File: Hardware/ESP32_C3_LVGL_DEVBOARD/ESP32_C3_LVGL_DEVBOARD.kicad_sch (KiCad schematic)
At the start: 62 parts, among them J1 CONN_USBC, J2 CONN_UART, J3 Conn_Coaxial, SW1 SW_Push_SPST_4Pads, SW2 SW_Push_SPST_4Pads, U2 USBLC6-2SC6, U3 AMS1117-3.3, U4 ESP32-C3, U5 Winbond-W25Q64JVSSIQ, U6 USBLC6-2SC6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

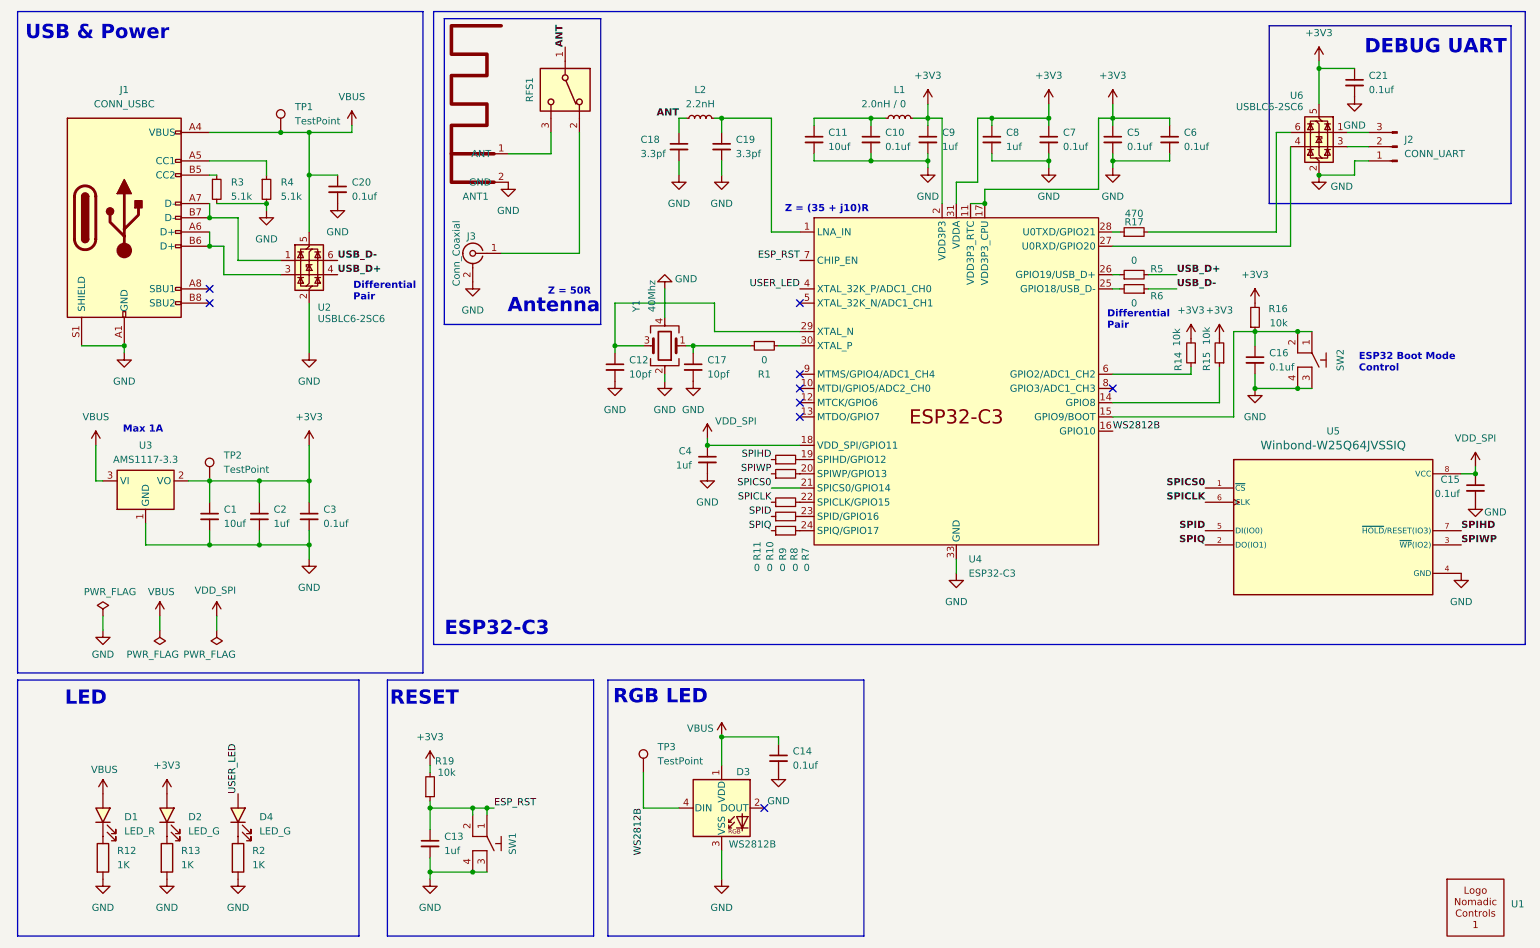
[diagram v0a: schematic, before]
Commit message: updated pcb with placement & basic routing
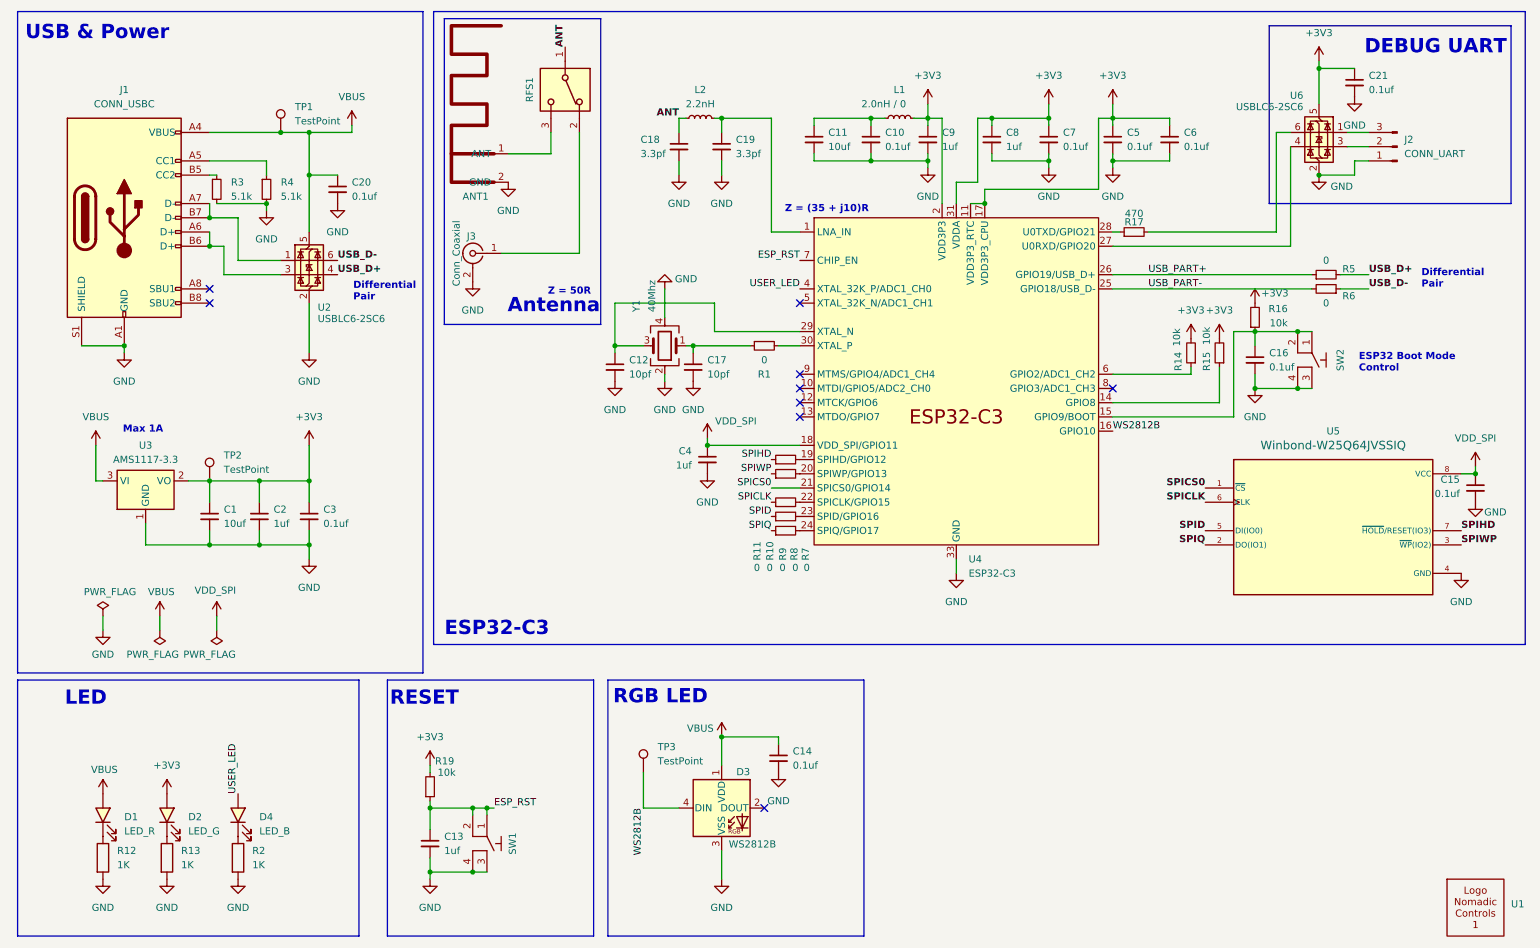
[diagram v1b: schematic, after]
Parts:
- C10, C14, C15, C16, C20, C21, C3, C5, C6, C7: footprint Capacitor_SMD:C_0805_2012Metric -> Capacitor_SMD:C_0603_1608Metric
- C12, C17: footprint Capacitor_SMD:C_0402_1005Metric -> Capacitor_SMD:C_0603_1608Metric
- D4: value LED_G -> LED_B
- L1: footprint Inductor_SMD:L_0805_2012Metric -> Inductor_SMD:L_0603_1608Metric
- R1, R10, R11, R12, R13, R14, R15, R16, R19, R2, R3, R4, R5, R6, R7, R8, R9: footprint Resistor_SMD:R_0805_2012Metric -> Resistor_SMD:R_0603_1608Metric
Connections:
- net USB_PART-: now reaches R6.2, U4.25 (GPIO18/USB_D-)
- net USB_PART+: now reaches R5.1, U4.26 (GPIO19/USB_D+)
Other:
- moved on the sheet: R5, R6
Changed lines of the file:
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@@
 	(wire
 		(pts
-			(xy 209.55 63.5) (xy 210.82 63.5)
+			(xy 209.55 63.5) (xy 245.11 63.5)
 		)
 		(stroke
@@
 	(wire
 		(pts
-			(xy 209.55 60.96) (xy 210.82 60.96)
+			(xy 209.55 60.96) (xy 245.11 60.96)
 		)
 		(stroke
@@
 	(wire
 		(pts
-			(xy 215.9 63.5) (xy 220.98 63.5)
+			(xy 250.19 63.5) (xy 255.27 63.5)
 		)
 		(stroke
@@
 	(wire
 		(pts
-			(xy 215.9 60.96) (xy 220.98 60.96)
+			(xy 250.19 60.96) (xy 255.27 60.96)
 		)
 		(stroke
@@
 	(text "Differential\nPair"
 		(exclude_from_sim no)
-		(at 208.534 69.088 0)
+		(at 264.668 61.722 0)
 		(effects
 			(font
@@
 		)
 	)
+	(label "USB_PART-"
+		(at 215.9 63.5 0)
+		(fields_autoplaced yes)
+		(effects
+			(font
+				(size 1.27 1.27)
+			)
+			(justify left bottom)
+		)
+	)
 	(label "USB_D-"
 		(at 71.12 58.42 0)
@@
 	)
 	(label "USB_D-"
-		(at 220.98 63.5 0)
+		(at 255.27 63.5 0)
 		(fields_autoplaced yes)
 		(effects
@@
 		)
 	)
+	(label "USB_PART+"
+		(at 215.9 60.96 0)
+		(fields_autoplaced yes)
+		(effects
+			(font
+				(size 1.27 1.27)
+			)
+			(justify left bottom)
+		)
+	)
 	(label "USER_LED"
 		(at 53.34 153.67 90)
@@
 	)
 	(label "USB_D+"
-		(at 220.98 60.96 0)
+		(at 255.27 60.96 0)
 		(fields_autoplaced yes)
 		(effects
@@
 			)
 		)
-		(property "Footprint" "Resistor_SMD:R_0805_2012Metric"
+		(property "Footprint" "Resistor_SMD:R_0603_1608Metric"
 			(at 49.53 45.72 0)
 			(effects
@@
 			)
 		)
-		(property "Footprint" "Capacitor_SMD:C_0402_1005Metric"
+		(property "Footprint" "Capacitor_SMD:C_0603_1608Metric"
 			(at 120.65 77.47 0)
 			(effects
@@
 			)
 		)
-		(property "Footprint" "Capacitor_SMD:C_0805_2012Metric"
+		(property "Footprint" "Capacitor_SMD:C_0603_1608Metric"
 			(at 166.37 36.83 0)
 			(effects
@@
 			)
 		)
-		(property "Footprint" "Capacitor_SMD:C_0805_2012Metric"
+		(property "Footprint" "Capacitor_SMD:C_0603_1608Metric"
 			(at 198.12 36.83 0)
 			(effects
@@
 			)
 		)
-		(property "Footprint" "Capacitor_SMD:C_0805_2012Metric"
+		(property "Footprint" "Capacitor_SMD:C_0603_1608Metric"
 			(at 66.04 104.14 0)
 			(effects
@@
 	(symbol
 		(lib_id "Device:R_Small")
-		(at 213.36 63.5 270)
+		(at 247.65 63.5 270)
 		(mirror x)
 		(unit 1)
@@
 		(dnp no)
 		(property "Reference" "R6"
-			(at 217.424 64.77 90)
+			(at 251.714 64.77 90)
 			(effects
 				(font
@@
 		)
 		(property "Value" "0"
-			(at 213.36 66.04 90)
+			(at 247.65 66.04 90)
 			(effects
 				(font
@@
 			)
 		)
-		(property "Footprint" "Resistor_SMD:R_0805_2012Metric"
-			(at 213.36 63.5 0)
+		(property "Footprint" "Resistor_SMD:R_0603_1608Metric"
+			(at 247.65 63.5 0)
 			(effects
 				(font
@@
 		)
 		(property "Datasheet" "~"
-			(at 213.36 63.5 0)
+			(at 247.65 63.5 0)
 			(effects
 				(font
@@
 		)
 		(property "Description" "Resistor, small symbol"
-			(at 213.36 63.5 0)
+			(at 247.65 63.5 0)
 			(effects
 				(font
@@
 			)
 		)
-		(property "Footprint" "Resistor_SMD:R_0805_2012Metric"
+		(property "Footprint" "Resistor_SMD:R_0603_1608Metric"
 			(at 151.13 96.52 0)
 			(effects
@@
 			)
 		)
-		(property "Footprint" "Resistor_SMD:R_0805_2012Metric"
+		(property "Footprint" "Resistor_SMD:R_0603_1608Metric"
 			(at 151.13 101.6 0)
 			(effects
@@
 			)
 		)
-		(property "Footprint" "Resistor_SMD:R_0805_2012Metric"
+		(property "Footprint" "Resistor_SMD:R_0603_1608Metric"
 			(at 151.13 93.98 0)
 			(effects
@@
 			)
 		)
-		(property "Footprint" "Resistor_SMD:R_0805_2012Metric"
+		(property "Footprint" "Resistor_SMD:R_0603_1608Metric"
 			(at 228.6 74.93 0)
 			(effects
@@
 			)
 		)
-		(property "Footprint" "Capacitor_SMD:C_0805_2012Metric"
+		(property "Footprint" "Capacitor_SMD:C_0603_1608Metric"
 			(at 209.55 36.83 0)
 			(effects
@@
 			)
 		)
-		(property "Footprint" "Resistor_SMD:R_0805_2012Metric"
+		(property "Footprint" "Resistor_SMD:R_0603_1608Metric"
 			(at 234.95 68.58 0)
 			(effects
@@
 			)
 		)
-		(property "Footprint" "Resistor_SMD:R_0805_2012Metric"
+		(property "Footprint" "Resistor_SMD:R_0603_1608Metric"
 			(at 147.32 73.66 0)
 			(effects
@@
 			)
 		)
-		(property "Footprint" "Capacitor_SMD:C_0805_2012Metric"
+		(property "Footprint" "Capacitor_SMD:C_0603_1608Metric"
 			(at 252.73 26.67 0)
 			(effects
@@
 			)
 		)
-		(property "Footprint" "Resistor_SMD:R_0805_2012Metric"
+		(property "Footprint" "Resistor_SMD:R_0603_1608Metric"
 			(at 27.432 165.1 90)
 			(effects
@@
 	(symbol
 		(lib_id "Device:R_Small")
-		(at 213.36 60.96 90)
+		(at 247.65 60.96 90)
 		(unit 1)
 		(exclude_from_sim no)
@@
 		(dnp no)
 		(property "Reference" "R5"
-			(at 217.424 59.944 90)
+			(at 251.714 59.944 90)
 			(effects
 				(font
@@
 		)
 		(property "Value" "0"
-			(at 213.36 58.42 90)
+			(at 247.65 58.42 90)
 			(effects
 				(font
@@
 			)
 		)
-		(property "Footprint" "Resistor_SMD:R_0805_2012Metric"
-			(at 213.36 60.96 0)
+		(property "Footprint" "Resistor_SMD:R_0603_1608Metric"
+			(at 247.65 60.96 0)
 			(effects
 				(font
@@
 		)
 		(property "Datasheet" "~"
-			(at 213.36 60.96 0)
+			(at 247.65 60.96 0)
 			(effects
 				(font
@@
 		)
 		(property "Description" "Resistor, small symbol"
-			(at 213.36 60.96 0)
+			(at 247.65 60.96 0)
 			(effects
 				(font
@@
 			)
 		)
-		(property "Footprint" "Resistor_SMD:R_0805_2012Metric"
+		(property "Footprint" "Resistor_SMD:R_0603_1608Metric"
 			(at 151.13 106.68 0)
 			(effects
@@
 			)
 		)
-		(property "Footprint" "Resistor_SMD:R_0805_2012Metric"
+		(property "Footprint" "Resistor_SMD:R_0603_1608Metric"
 			(at 223.52 74.93 0)
 			(effects
@@
 			)
 		)
-		(property "Value" "LED_G"
+		(property "Value" "LED_B"
 			(at 57.15 160.3374 90)
 			(effects
@@
 			)
 		)
-		(property "Footprint" "Capacitor_SMD:C_0805_2012Metric"
+		(property "Footprint" "Capacitor_SMD:C_0603_1608Metric"
 			(at 234.95 76.2 0)
 			(effects
@@
 		)
 		(property "Value" "+3V3"
-			(at 234.95 60.96 0)
+			(at 238.506 64.262 0)
 			(effects
 				(font
@@
 			)
 		)
-		(property "Footprint" "Capacitor_SMD:C_0402_1005Metric"
+		(property "Footprint" "Capacitor_SMD:C_0603_1608Metric"
 			(at 134.62 77.47 0)
 			(effects
@@
 			)
 		)
-		(property "Footprint" "Resistor_SMD:R_0805_2012Metric"
+		(property "Footprint" "Resistor_SMD:R_0603_1608Metric"
 			(at 38.862 165.1 90)
 			(effects
@@
 			)
 		)
-		(property "Footprint" "Capacitor_SMD:C_0805_2012Metric"
+		(property "Footprint" "Capacitor_SMD:C_0603_1608Metric"
 			(at 274.32 99.06 0)
 			(effects
@@
 			)
 		)
-		(property "Footprint" "Resistor_SMD:R_0805_2012Metric"
+		(property "Footprint" "Resistor_SMD:R_0603_1608Metric"
 			(at 87.63 152.4 0)
 			(effects
@@
 			)
 		)
-		(property "Footprint" "Inductor_SMD:L_0805_2012Metric"
+		(property "Footprint" "Inductor_SMD:L_0603_1608Metric"
 			(at 171.45 33.02 0)
 			(effects
@@
 			)
 		)
-		(property "Footprint" "Resistor_SMD:R_0805_2012Metric"
+		(property "Footprint" "Resistor_SMD:R_0603_1608Metric"
 			(at 151.13 104.14 0)
 			(effects
@@
 			)
 		)
-		(property "Footprint" "Resistor_SMD:R_0805_2012Metric"
+		(property "Footprint" "Resistor_SMD:R_0603_1608Metric"
 			(at 58.42 45.72 0)
 			(effects
@@
 			)
 		)
-		(property "Footprint" "Resistor_SMD:R_0805_2012Metric"
+		(property "Footprint" "Resistor_SMD:R_0603_1608Metric"
 			(at 51.562 165.1 90)
 			(effects
@@
 			)
 		)
-		(property "Footprint" "Capacitor_SMD:C_0805_2012Metric"
+		(property "Footprint" "Capacitor_SMD:C_0603_1608Metric"
 			(at 149.86 147.32 0)
 			(effects
@@
 			)
 		)
-		(property "Footprint" "Capacitor_SMD:C_0805_2012Metric"
+		(property "Footprint" "Capacitor_SMD:C_0603_1608Metric"
 			(at 71.12 45.72 0)
 			(effects
@@
 			)
 		)
-		(property "Footprint" "Capacitor_SMD:C_0805_2012Metric"
+		(property "Footprint" "Capacitor_SMD:C_0603_1608Metric"
 			(at 219.71 36.83 0)
 			(effects
